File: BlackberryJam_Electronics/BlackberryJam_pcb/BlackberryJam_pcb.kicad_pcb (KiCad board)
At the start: 2 copper layers, 6 parts, among them U2 ARDUINO_PRO_MINI, U4 MMA8452_Breakout, U5 Motor_Driver_Dual_TB6612FNG

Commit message: PCB Layout with components
1. Updated and assigned footprints in schematic
2. Placed components on PCB editor

Note:
No connection is made in the PCB now
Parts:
- added M2: PUMP2, Connector_PinHeader_2.54mm:PinHeader_1x02_P2.54mm_Vertical, F.Cu at (7.62, 17.8)
- added M3: CONTROL GROUP MOTOR, Connector_PinHeader_2.54mm:PinHeader_1x02_P2.54mm_Vertical, F.Cu at (45.7, 61.0)
- added U1: HW-107_Breakout, Connector_PinHeader_2.54mm:PinHeader_1x02_P2.54mm_Vertical, F.Cu at (45.7, 5.08)
- added U3: Slip_Ring, Connector_PinHeader_2.54mm:PinHeader_1x02_P2.54mm_Vertical, F.Cu at (31.8, 61.0)
- moved U2 137.0 mm to (40.6, 30.5), turned to -90 degrees
- moved D2 103.9 mm to (6.35, 12.7)
- moved U5 88.3 mm to (8.98, 64.7)
- moved D1 77.0 mm to (31.8, 50.8)
- moved D3 44.5 mm to (45.7, 50.8)
- moved U4 9.95 mm to (30.5, 18.0)
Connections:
- D1 pad 2: Net-(D1-Pad2) -> Net-(D2-Pad1)
- D2 pad 2: Net-(D2-Pad2) -> Net-(D1-Pad1)
- U5 pad 5: Net-(D2-Pad2) -> Net-(D1-Pad1)

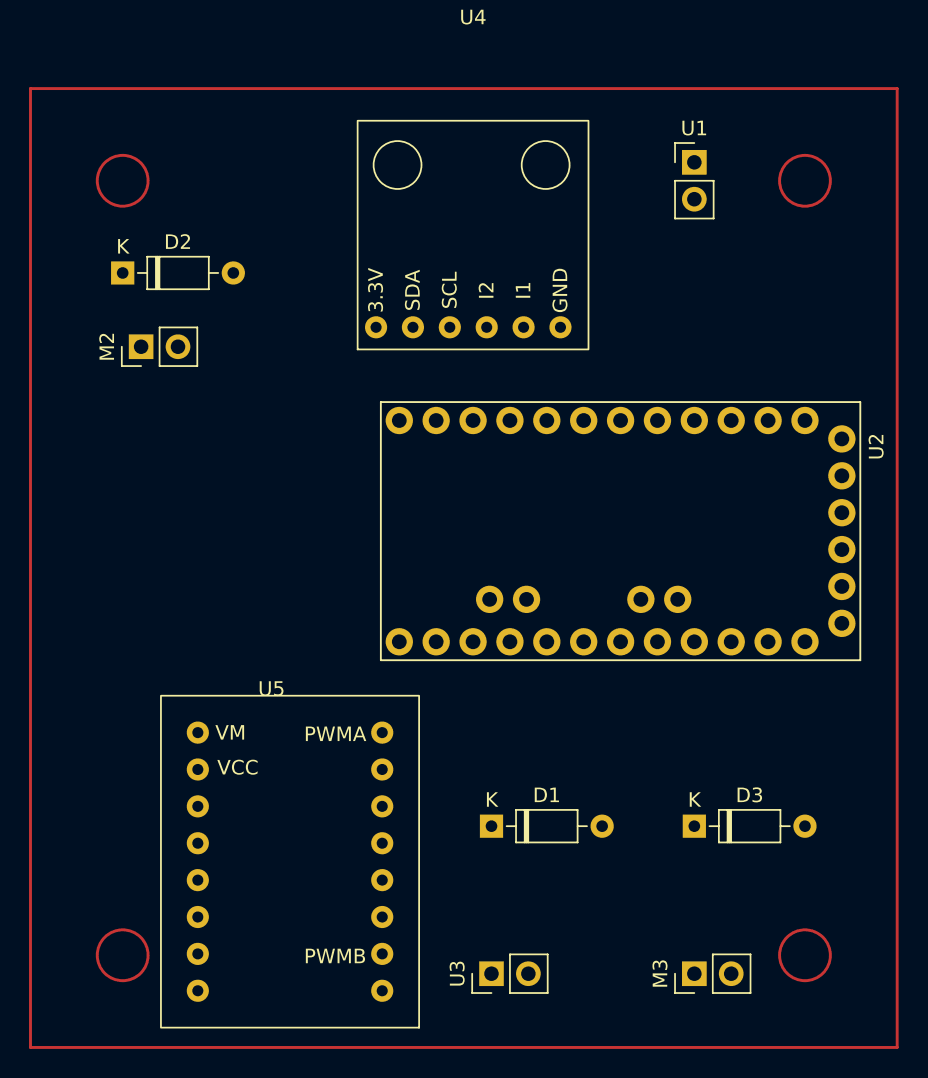
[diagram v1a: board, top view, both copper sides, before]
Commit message: PCB Update w/ Trace
1. All traces has been made with ground plane on two side of the board
2. Clearance and dimensions follows the limitation of JLCPCB
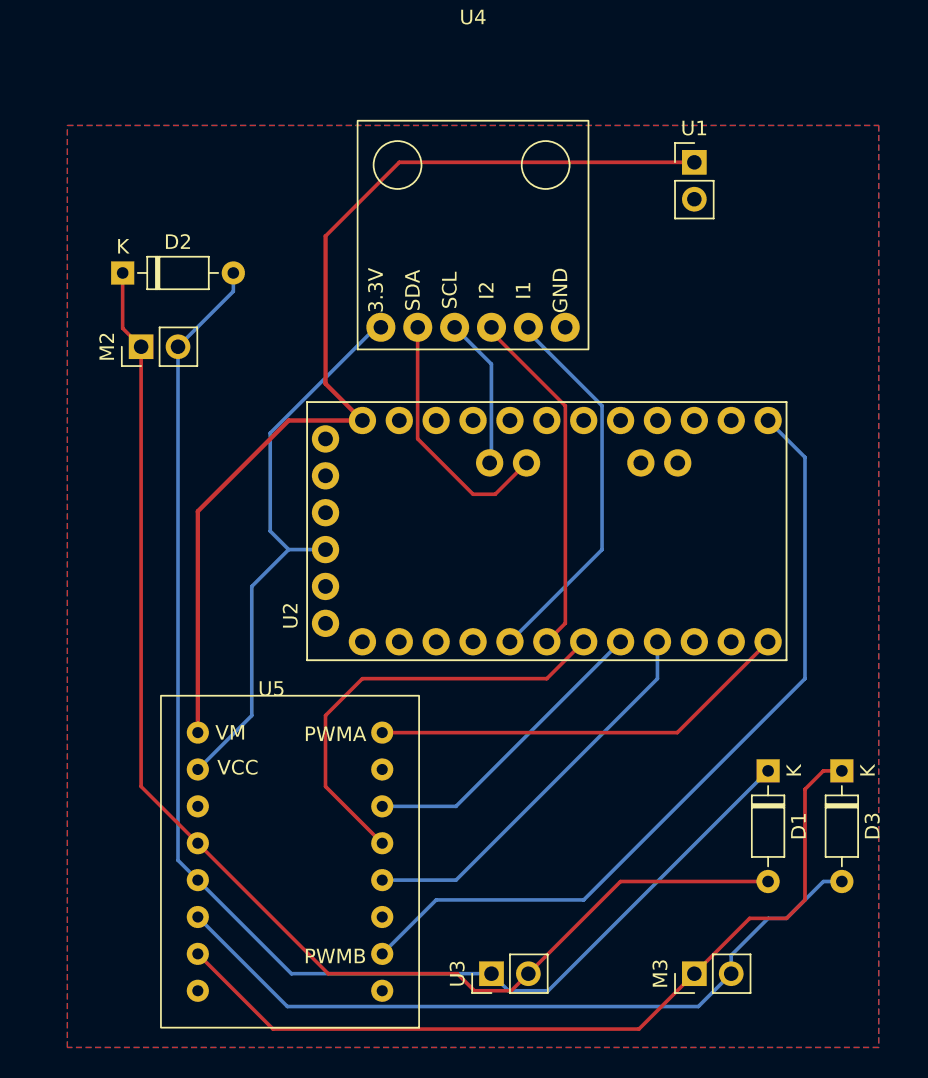
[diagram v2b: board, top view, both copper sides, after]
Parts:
- moved D1 19.4 mm to (50.8, 47.0), turned to -90 degrees
- moved D3 10.9 mm to (55.9, 47.0), turned to -90 degrees
- moved U2 5.08 mm to (35.6, 30.5), turned to 90 degrees
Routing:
- net Net-(D1-Pad1): track 0.00 -> 92.7 mm
- net Net-(D1-Pad2): track 0.00 -> 88.0 mm
- net RAW (V_IN): track 0.00 -> 70.4 mm
- net Net-(D3-Pad1): track 0.00 -> 58.6 mm
- net D10 (PWM): track 0.00 -> 55.8 mm
- net Net-(D3-Pad2): track 0.00 -> 51.2 mm
- net VCC (3.3V): track 0.00 -> 39.1 mm
- net D4: track 0.00 -> 30.3 mm
- net D9 (PWM): track 0.00 -> 29.2 mm
- net D6: track 0.00 -> 27.2 mm
- net D2 (INT0): track 0.00 -> 26.5 mm
- net D3 (INT1): track 0.00 -> 24.4 mm
- net D5: track 0.00 -> 21.1 mm
- net A4: track 0.00 -> 17.8 mm
- net A5: track 0.00 -> 11.7 mm
- added copper zone on B.Cu, net GND
- added copper zone on F.Cu, net GND

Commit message: SCH and PCB Update
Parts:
- removed D3: 1N4148, Diode_THT:D_DO-35_SOD27_P7.62mm_Horizontal
- added HVR 2022 XENIA-1 : LOGO, LOGO, B.Cu at (5.08, 27.9)
- D1, D2: footprint Diode_THT:D_DO-35_SOD27_P7.62mm_Horizontal -> Diode_SMD:D_0805_2012Metric
- U2: value ARDUINO_PRO_MINI -> ARDUINO PRO MINI
- U4: value MMA8452_Breakout -> MMA8452Q
- U5: value Motor_Driver_Dual_TB6612FNG -> MOTOR DRIVER
- moved D2 56.0 mm to (48.6, 49.5)
- moved M2 52.1 mm to (44.5, 54.6), turned to -90 degrees
- moved U1 29.3 mm to (16.5, 7.62), turned to 180 degrees
- moved U4 14.3 mm to (30.5, 3.65), turned to 180 degrees
- moved D1 12.6 mm to (38.4, 49.5), turned to 0 degrees
- moved U3 8.13 mm to (36.8, 54.6)
- moved M3 6.48 mm to (47.0, 54.6)
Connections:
- D2 pad 1: Net-(D1-Pad2) -> Net-(D2-Pad1)
- D2 pad 2: Net-(D1-Pad1) -> Net-(D2-Pad2)
- M2 pad 1: Net-(D1-Pad2) -> Net-(D1-Pad1)
- M2 pad 2: Net-(D1-Pad1) -> Net-(D1-Pad2)
- M3 pad 1: Net-(D3-Pad1) -> Net-(D2-Pad1)
- M3 pad 2: Net-(D3-Pad2) -> Net-(D2-Pad2)
- U5 pad 6: Net-(D3-Pad2) -> Net-(D2-Pad2)
- U5 pad 7: Net-(D3-Pad1) -> Net-(D2-Pad1)
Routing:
- net Net-(D3-Pad1): track 58.6 -> 0.00 mm
- net Net-(D2-Pad2): track 0.00 -> 53.0 mm
- net Net-(D3-Pad2): track 51.2 -> 0.00 mm
- net Net-(D2-Pad1): track 0.00 -> 50.1 mm
- net Net-(D1-Pad1): track 92.7 -> 47.9 mm
- net Net-(D1-Pad2): track 88.0 -> 44.2 mm
- net VCC (3.3V): track 39.1 -> 68.8 mm
- net RAW (V_IN): track 70.4 -> 47.0 mm
- net D3 (INT1): track 24.4 -> 36.1 mm
- net D2 (INT0): track 26.5 -> 37.1 mm
- net A5: track 11.7 -> 21.8 mm
- net A4: track 17.8 -> 22.1 mm
- net D10 (PWM): track 55.8 -> 58.0 mm
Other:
- board text added: "BLACKBERRY JAM PCB"
- board text added: "MADE BY GORDON SO"
